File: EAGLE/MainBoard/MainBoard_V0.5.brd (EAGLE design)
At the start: 36.8 x 104.1 mm, 34 parts, among them IC2 CEM3340

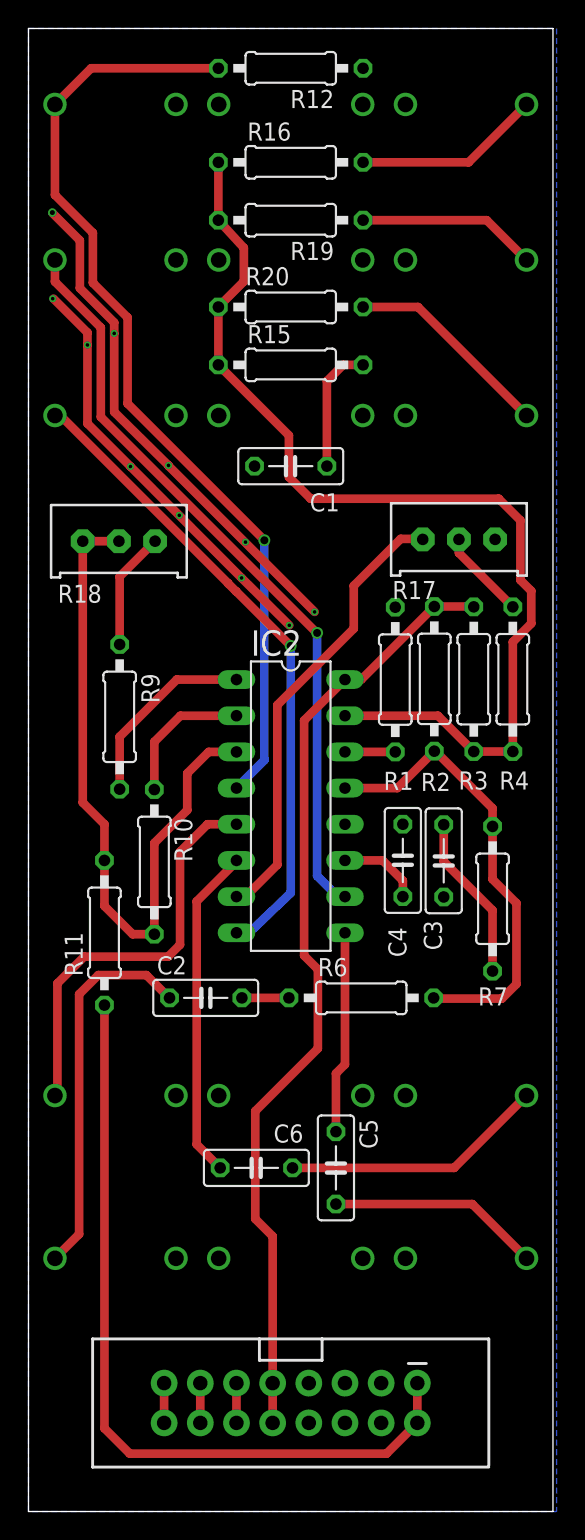
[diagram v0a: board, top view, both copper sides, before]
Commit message: Renumber Parts
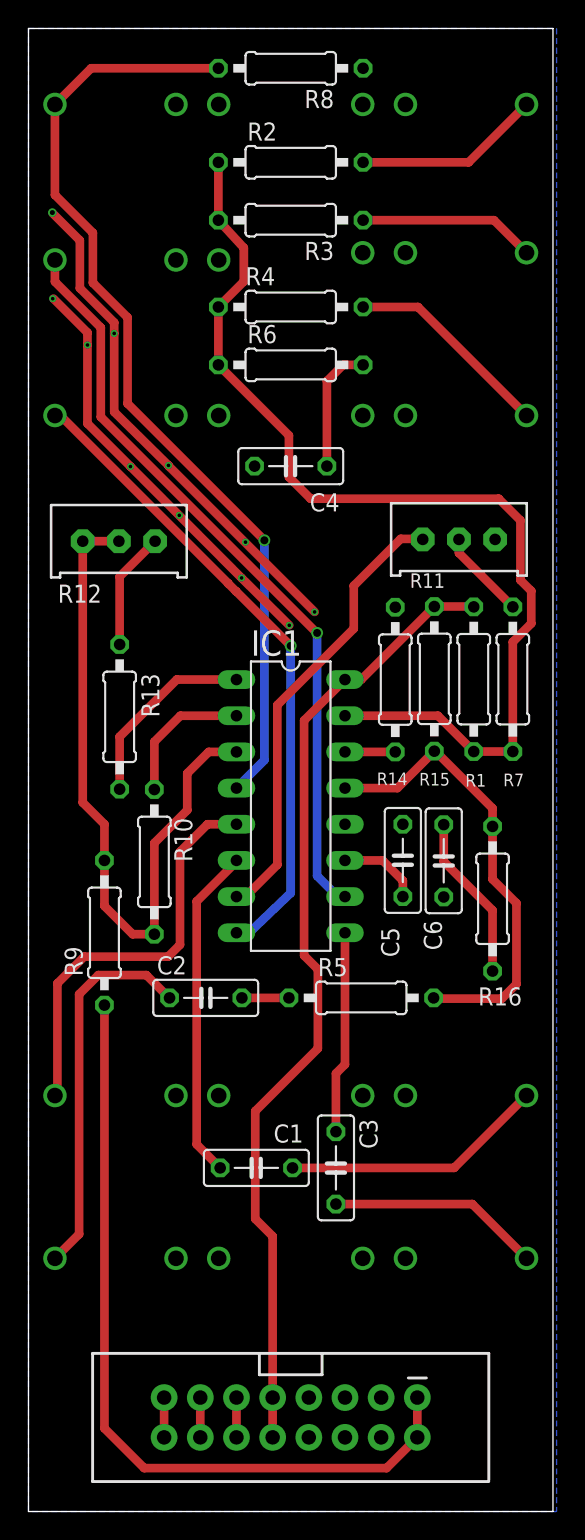
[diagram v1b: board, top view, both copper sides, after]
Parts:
- removed J3: (no value), SparkFun-Connectors:2X8-SHROUDED_LOCK
- removed R17: 20K, bourns:3386W
- removed R18: 10K, bourns:3386W
- removed R19, R20: 100K, rcl:0207/10
- added J8: (no value), SparkFun-Connectors:2X8-SHROUDED_LOCK
- added R13: 24KΩ, rcl:0207/10
- added R14: 1.8KΩ, rcl:0207/10
- added R5: 1MΩ, rcl:0207/10
- added R8: 10KΩ, rcl:0207/10
- C1, C3: value 0.01μF -> 0.001μF
- C4: value 1000pF -> 0.01μF
- C6: value 0.001μF -> 0.01μF
- R1: value 1.8K -> 360KΩ
- R10: value 5.6K -> 5.6KΩ
- R11: value 600 -> 20KΩ; device rcl:0207/10 -> bourns:3386W
- R12: value 10K -> 10KΩ; device rcl:0207/10 -> bourns:3386W
- R15: value 470 -> 1.5MΩ
- R16: value 100K -> 470Ω
- R2: value 1.5M -> 100KΩ
- R3: value 360K -> 100KΩ
- R4: value 1M -> 100KΩ
- R6: value 1M -> 470Ω
- R7: value 470 -> 1MΩ
- R9: value 24K -> 600Ω
- moved R16 53.6 mm to (32.6, 43.0), turned to 270 degrees
- moved C1 49.3 mm to (16.0, 24.1)
- moved R6 44.7 mm to (18.4, 80.5)
- moved R2 37.6 mm to (18.4, 94.7), turned to 0 degrees
- moved R11 37.4 mm to (30.2, 68.6), turned to 180 degrees
- moved R12 35.0 mm to (6.35, 68.5)
- moved R3 34.7 mm to (18.4, 90.7), turned to 180 degrees
- moved R4 30.4 mm to (18.4, 84.6), turned to 180 degrees
- moved C4 28.8 mm to (18.4, 73.4), turned to 180 degrees
- moved C6 25.3 mm to (29.2, 45.7), turned to 270 degrees
- moved R15 24.2 mm to (28.5, 58.5), turned to 270 degrees
- moved C3 22.9 mm to (21.6, 24.1)
- moved C5 22.1 mm to (26.3, 45.7), turned to 90 degrees
- moved R7 15.5 mm to (34.0, 58.4), turned to 90 degrees
- moved R9 15.2 mm to (5.33, 40.6), turned to 90 degrees
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- renumbered IC2 to IC1, LINEAR-FM to LIN_FM, PWM_C to PWM
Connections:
- net +12V: now also J8.10, J8.9, R1.1, R15.1; no longer J3.10, J3.9, R2.1, R3.1
- net +5V: now also J8.11, J8.12; no longer J3.11, J3.12
- net -12V: now also J8.1, J8.2, R9.1; no longer J3.1, J3.2, R11.1
- net CV: now also J8.13, J8.14; no longer J3.13, J3.14
- net FCTL: now also R1.2, R2.1, R4.2, R6.1, R7.1; no longer R15.1, R16.1, R19.2, R20.2, R4.1
- net GATE: now also J8.15, J8.16; no longer J3.15, J3.16
- net GND: now also C5.2, C6.2, J8.3, J8.4, J8.5, J8.6, J8.7, J8.8, R11.3, R14.1, R8.1; no longer C1.2, C3.2, J3.3, J3.4, J3.5, J3.6, J3.7, J3.8, R1.1, R12.1, R17.3
- net HARD_S: now also C1.2; no longer C6.2
- net LIN_FM: now also R15.2, R16.1, R5.2; no longer R2.2, R6.2, R7.1
- net N$10: now also R11.2, R7.2; no longer R17.2, R4.2
- net N$11: now also R12.3, R13.1; no longer R18.3, R9.1
- net N$13: now also R11.1; no longer R17.1
- net N$14: now also R2.2; no longer R16.2
- net N$15: now also R12.1, R12.2, R9.2; no longer R11.2, R18.1, R18.2
- net N$16: now also C1.1; no longer C6.1
- net N$2: now also C4.1, R6.2; no longer C1.1, R15.2
- net N$20: now also R3.1; no longer R19.1
- net N$22: now also R4.1; no longer R20.1
- net N$29: now also C3.2; no longer C5.2
- net N$3: now also R14.2; no longer R1.2
- net N$5: now also R5.1; no longer R6.1
- net N$6: now also C6.1, R16.2; no longer C3.1, R7.2
- net N$7: now also C5.1; no longer C4.1
- net N$8: now also R13.2; no longer R9.2
- net SOFT_S: now also C3.1; no longer C5.1
- net SQUARE: now also R8.2; no longer R12.2
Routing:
- net +12V: track 67.3 -> 68.3 mm

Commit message: Logo, Top Ground Planes
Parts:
- moved R5 2.03 mm to (21.3, 36.1)
- moved C2 1.52 mm to (10.9, 36.1)
- moved C3 1.02 mm to (20.6, 24.1)
- moved C1 0.51 mm to (16.5, 24.1), turned to 90 degrees
- turned C6 to 90 degrees
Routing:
- net N$6: track 11.7 -> 6.63 mm
- net N$16: track 18.5 -> 21.6 mm
- net LIN_FM: track 32.4 -> 34.4 mm
- net +12V: track 68.3 -> 69.9 mm
- net HARD_S: track 23.4 -> 22.2 mm
- net N$29: track 15.0 -> 16.0 mm
- net -12V: track 56.5 -> 57.3 mm
- net SAW: track 45.5 -> 46.3 mm
- net N$5: track 3.30 -> 2.79 mm
- net GND: vias 11 -> 18
- added copper zone on layer 1, net GND
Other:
- board text added: "EuroRack MainBoard V0.5"
- board text added: "https://github.com/freesideatlanta/EuroRack_CEM3340"
